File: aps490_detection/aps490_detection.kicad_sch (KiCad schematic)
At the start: 0 parts

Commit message: Link Nucleo32 into main HW project
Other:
- added sheet Detection_Circuit (detection_circuit.kicad_sch)
- added sheet U_MB1180_NUCLEO32 (../MB1180/MB1180-SchDoc.kicad_sch)
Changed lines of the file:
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@@
     (company "PFPU2")
+  )
+  (sheet (at 22.86 156.21) (size 118.11 30.48) (fields_autoplaced)
+    (stroke (width 0.1524) (type solid))
+    (fill (color 0 0 0 0.0000))
+    (property "Sheetname" "U_MB1180_NUCLEO32" (at 22.86 155.4984 0)
+      (effects (font (size 1.27 1.27)) (justify left bottom))
+    )
+    (property "Sheetfile" "../MB1180/MB1180-SchDoc.kicad_sch" (at 22.86 187.2746 0)
+      (effects (font (size 1.27 1.27)) (justify left top))
+    )
+    (instances
+      (project "MB1180"
+        (path "/a2ef7e76-e1f0-4b38-892b-f0f108e628a0" (page "2"))
+      )
+      (project "aps490_detection"
+        (path "/e118c919-9296-4265-a7f4-7c13f94290b1" (page "#"))
+      )
+    )
+  )
+  (sheet (at 96.52 63.5) (size 92.71 57.15) (fields_autoplaced)
+    (stroke (width 0.1524) (type solid))
+    (fill (color 0 0 0 0.0000))
+    (property "Sheetname" "Detection_Circuit" (at 96.52 62.7884 0)
+      (effects (font (size 1.27 1.27)) (justify left bottom))
+    )
+    (property "Sheetfile" "detection_circuit.kicad_sch" (at 96.52 121.2346 0)
+      (effects (font (size 1.27 1.27)) (justify left top))
+    )
+    (instances
+      (project "aps490_detection"
+        (path "/e118c919-9296-4265-a7f4-7c13f94290b1" (page "5"))
+      )
+    )
   )
   (sheet_instances

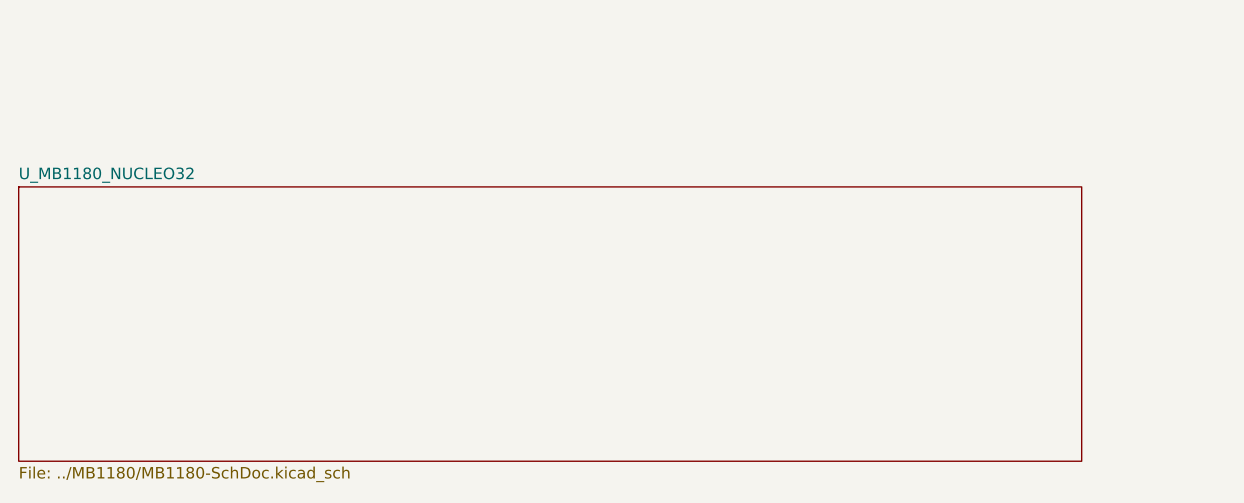
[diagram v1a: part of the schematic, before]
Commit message: add lipo charger
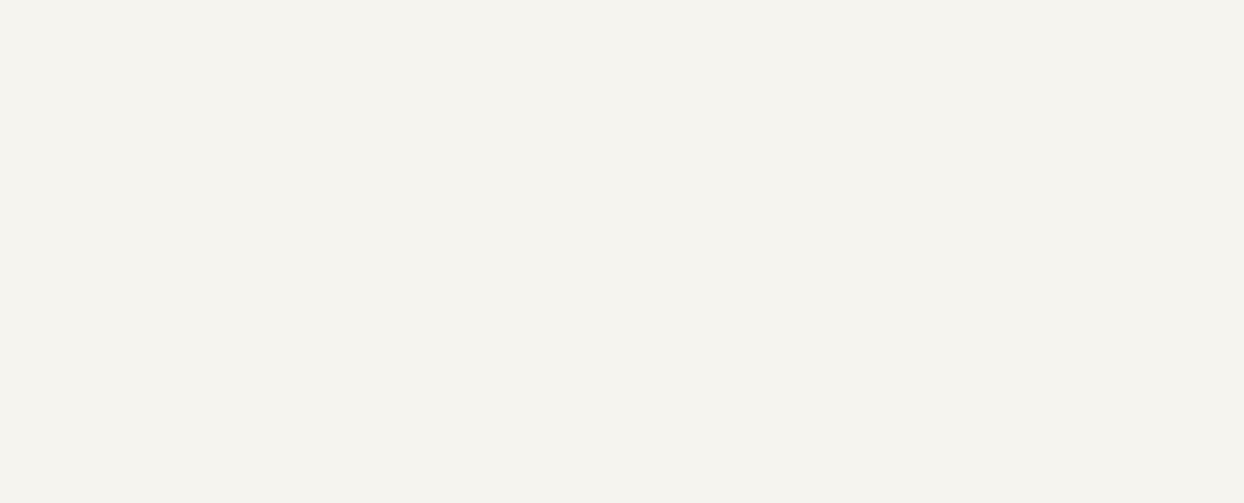
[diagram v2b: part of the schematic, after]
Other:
- removed sheet U_MB1180_NUCLEO32
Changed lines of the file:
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@@
     (company "PFPU2")
-  )
-  (sheet (at 22.86 156.21) (size 118.11 30.48) (fields_autoplaced)
-    (stroke (width 0.1524) (type solid))
-    (fill (color 0 0 0 0.0000))
-    (property "Sheetname" "U_MB1180_NUCLEO32" (at 22.86 155.4984 0)
-      (effects (font (size 1.27 1.27)) (justify left bottom))
-    )
-    (property "Sheetfile" "../MB1180/MB1180-SchDoc.kicad_sch" (at 22.86 187.2746 0)
-      (effects (font (size 1.27 1.27)) (justify left top))
-    )
-    (instances
-      (project "MB1180"
-        (path "/a2ef7e76-e1f0-4b38-892b-f0f108e628a0" (page "2"))
-      )
-      (project "aps490_detection"
-        (path "/e118c919-9296-4265-a7f4-7c13f94290b1" (page "#"))
-      )
-    )
   )
   (sheet (at 96.52 63.5) (size 92.71 57.15) (fields_autoplaced)

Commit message: update schematic
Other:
- title: Detection Mechanism -> Autopsy Saw Detection Mechanism
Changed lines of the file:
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@@
   (paper "A4")
   (title_block
-    (title "Detection Mechanism")
+    (title "Autopsy Saw Detection Mechanism")
+    (date "2024-03-24")
+    (rev "3")
     (company "PFPU2")
   )
@@
     (instances
       (project "aps490_detection"
-        (path "/e118c919-9296-4265-a7f4-7c13f94290b1" (page "5"))
+        (path "/e118c919-9296-4265-a7f4-7c13f94290b1" (page "2"))
       )
     )
